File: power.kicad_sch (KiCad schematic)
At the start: 0 parts

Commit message: Setup charging
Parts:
- added BT1: Battery_Cell, Connector_JST:JST_PH_S2B-PH-K_1x02_P2.00mm_Horizontal, symbol Device:Battery_Cell
- added C7: C, symbol Device:C
- added C8, C9: 4.7u, symbol Device:C
- added D1: D, symbol Device:D
- added D2: LED, symbol Device:LED
- added F1: Fuse, symbol Device:Fuse
- added J2: USB_C_Receptacle, Connector_USB:USB_C_Receptacle_GCT_USB4105-xx-A_16P_TopMnt_Horizontal, symbol Connector:USB_C_Receptacle
- added Q1, Q2: Q_NMOS_GSD, Package_TO_SOT_SMD:TSOT-23, symbol Device:Q_NMOS_GSD
- added R1, R2: 5.1k, symbol Device:R
- added R3: 220, symbol Device:R
- added R4: 2k, symbol Device:R
- added R5: R, symbol Device:R
- added R6: 470, symbol Device:R
- added U2: ~, Package_TO_SOT_SMD:SOT-23-5, symbol generic:Battery_Management
- added U3: MCP73831-2-OT, Package_TO_SOT_SMD:SOT-23-5, symbol Battery_Management:MCP73831-2-OT
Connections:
- new net: D2.1 (K), R6.1
- new net: D2.2 (A), U3.1 (STAT)
- new net: Q2.1 (G), U2.4 (DO)
- new net: Q1.3 (D), Q2.3 (D)
- new net: R5.1, U3.5 (PROG)
- new net: J2.B5 (CC2), R2.1
- new net: R4.2, U2.1 (VM)
- new net: C7.1, R3.1, U2.2 (VDD)
- new net: BT1.2 (-), F1.2
- new net: J2.A5 (CC1), R1.1
- new net: Q1.1 (G), U2.5 (CO)
- new net +BATT: BT1.1 (+), C8.1, D1.1 (K), R3.2, U3.3 (V_{BAT})
- new net -BATT: C7.2, D1.2 (A), F1.1, Q2.2 (S), U2.3 (VSS)
- new net D+: J2.A6 (D+), J2.B6 (D+)
- new net D-: J2.A7 (D-), J2.B7 (D-)
- new net GND: C8.2, C9.2, J2.A1 (GND), J2.A12 (GND), J2.B1 (GND), J2.B12 (GND), Q1.2 (S), R1.2, R2.2, R4.1, R5.2, R6.2, U3.2 (V_{SS})
- new net VBUS: C9.1, J2.A4 (VBUS), J2.A9 (VBUS), J2.B4 (VBUS), J2.B9 (VBUS), U3.4 (V_{DD})

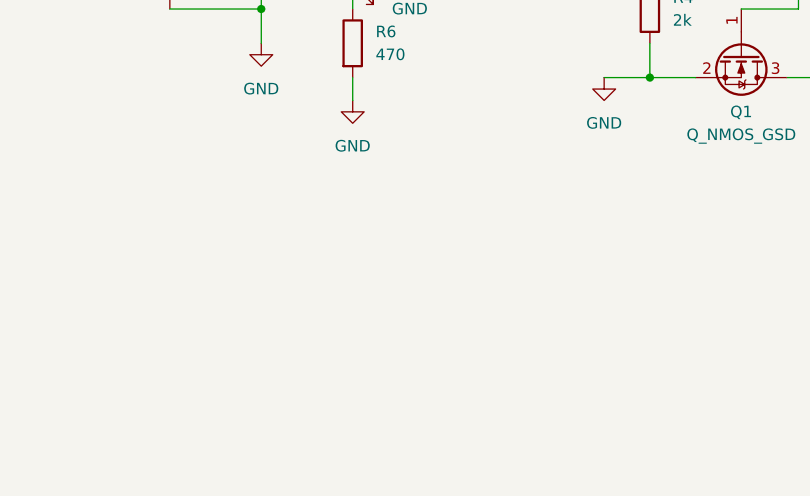
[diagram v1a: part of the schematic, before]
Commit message: Added outputs page
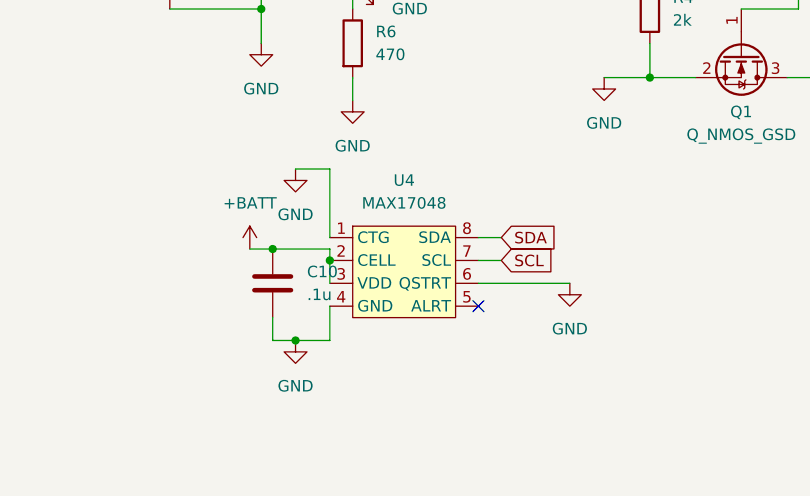
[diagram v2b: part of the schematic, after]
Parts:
- added C10: .1u, symbol Device:C
- added U4: MAX17048, Package_DFN_QFN:TDFN-8-1EP_2x2mm_P0.5mm_EP0.8x1.2mm, symbol generic:MAX17048
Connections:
- net +BATT: now also C10.1, U4.2 (CELL), U4.3 (VDD)
- net GND: now also C10.2, U4.1 (CTG), U4.4 (GND), U4.6 (QSTRT)
- new net SCL: U4.7 (SCL)
- new net SDA: U4.8 (SDA)
- no-connect marks 0 -> 1

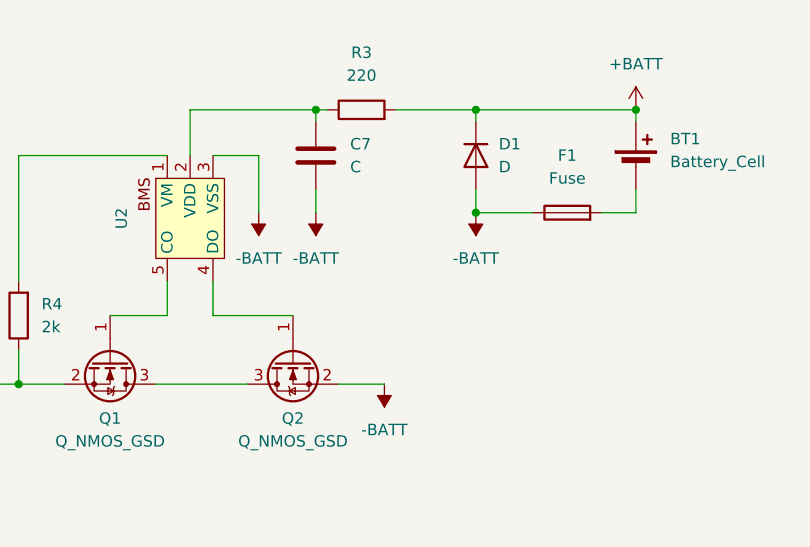
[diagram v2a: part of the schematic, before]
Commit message: Added output headers
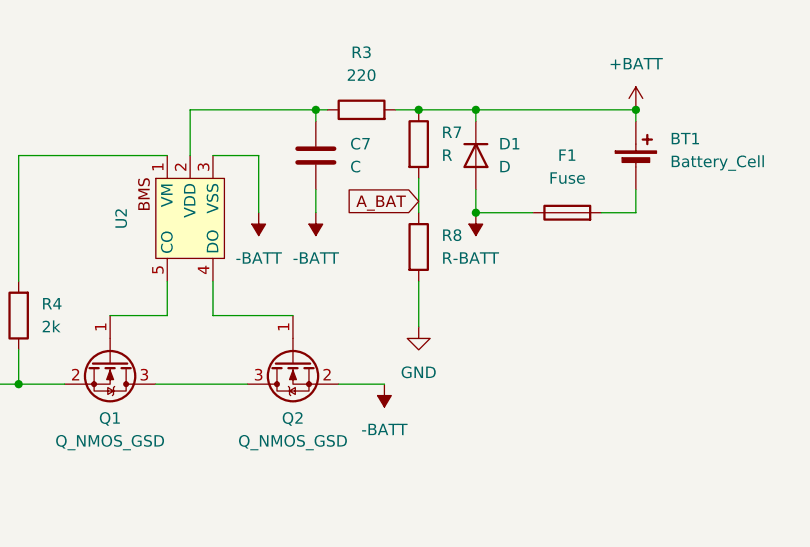
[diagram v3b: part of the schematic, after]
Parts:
- added R7, R8: R, symbol Device:R
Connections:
- net +BATT: now also R7.1
- net GND: now also R8.2
- new net A_BAT: R7.2, R8.1

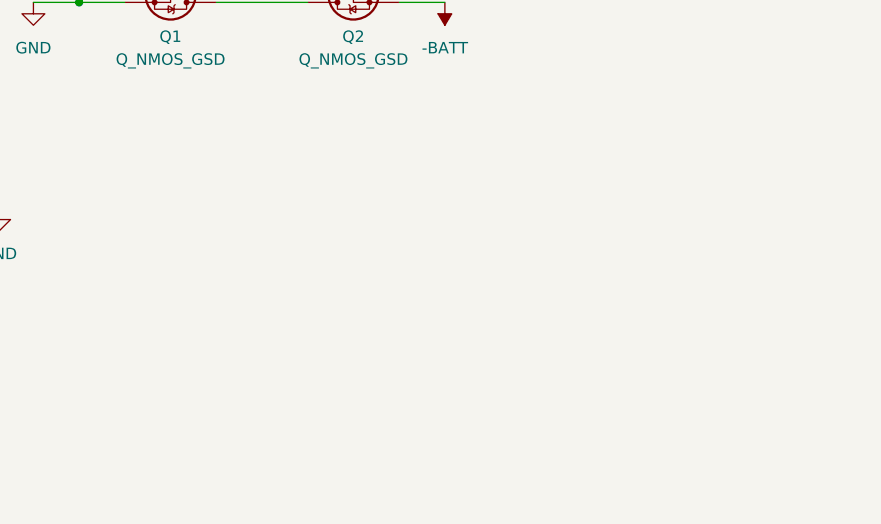
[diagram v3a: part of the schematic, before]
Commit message: Added pmos and regulator
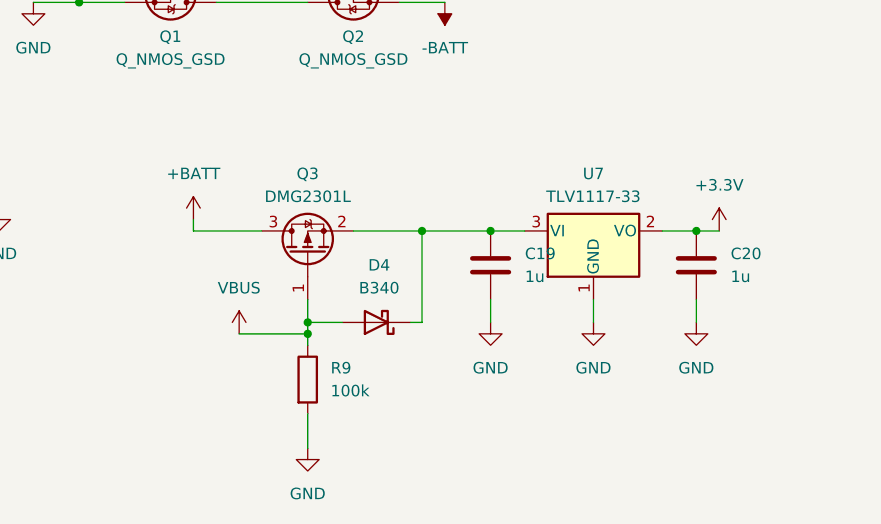
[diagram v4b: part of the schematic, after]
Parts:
- added C19, C20: 1u, symbol Device:C
- added D4: B340, Diode_SMD:D_SMC, symbol Diode:B340
- added Q3: DMG2301L, Package_TO_SOT_SMD:SOT-23, symbol Transistor_FET:DMG2301L
- added R9: 100k, symbol Device:R
- added U7: TLV1117-33, Package_TO_SOT_SMD:SOT-223-3_TabPin2, symbol Regulator_Linear:TLV1117-33
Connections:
- net +BATT: now also Q3.3 (D)
- net GND: now also C19.2, C20.2, R9.2, U7.1 (GND)
- net VBUS: now also D4.2 (A), Q3.1 (G), R9.1
- new net: C19.1, D4.1 (K), Q3.2 (S), U7.3 (VI)
- new net +3.3V: C20.1, U7.2 (VO)

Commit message: Switch regulator to 1.5A
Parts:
- removed U7: TLV1117-33, Package_TO_SOT_SMD:SOT-223-3_TabPin2, symbol Regulator_Linear:TLV1117-33
- added U8: LD39150DT33, Package_TO_SOT_SMD:TO-252-3_TabPin2, symbol Regulator_Linear:LD39150DT33
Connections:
- net +3.3V: now also U8.3 (VO)
- net GND: now also U8.2 (GND)
- net at C19.1, D4.1 (K), Q3.2 (S): now also U8.1 (VI)
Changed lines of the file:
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@@
-	)
-	(symbol
-		(lib_id "Regulator_Linear:TLV1117-33")
-		(at 226.06 87.63 0)
-		(unit 1)
-		(exclude_from_sim no)
-		(in_bom yes)
-		(on_board yes)
-		(dnp no)
-		(fields_autoplaced yes)
-		(property "Reference" "U7"
-			(at 226.06 81.28 0)
-			(effects
-				(font
-					(size 1.27 1.27)
-				)
-			)
-		)
-		(property "Value" "TLV1117-33"
-			(at 226.06 83.82 0)
-			(effects
-				(font
-					(size 1.27 1.27)
-				)
-			)
-		)
-		(property "Footprint" "Package_TO_SOT_SMD:SOT-223-3_TabPin2"
-			(at 226.06 87.63 0)
-			(effects
-				(font
-					(size 1.27 1.27)
-				)
-				(hide yes)
-			)
-		)
-		(property "Datasheet" "http://www.ti.com/lit/ds/symlink/tlv1117.pdf"
-			(at 226.06 87.63 0)
-			(effects
-				(font
-					(size 1.27 1.27)
-				)
-				(hide yes)
-			)
-		)
-		(property "Description" "800mA Low-Dropout Linear Regulator, 3.3V fixed output, TO-220/TO-252/TO-263/SOT-223"
-			(at 226.06 87.63 0)
-			(effects
-				(font
-					(size 1.27 1.27)
-				)
-				(hide yes)
-			)
-		)
-		(property "LCSC PN" "C15578"
-			(at 226.06 87.63 0)
-			(effects
-				(font
-					(size 1.27 1.27)
-				)
-				(hide yes)
-			)
-		)
-		(property "Part Number" "TLV1117LV33DCYR"
-			(at 226.06 87.63 0)
-			(effects
-				(font
-					(size 1.27 1.27)
-				)
-				(hide yes)
-			)
-		)
-		(pin "1"
-		)
-		(pin "3"
-		)
-		(pin "2"
-		)
-		(instances
-			(project ""
-				(path "/4b478080-1b18-4cae-a6eb-51454cf43595/0dd7376e-3e01-470b-b555-85887cf9232f"
-					(reference "U7")
-					(unit 1)
-				)
-			)
-		)
 	)
 	(symbol
@@
 					(unit 1)
 				)
+			)
+		)
+	)
+	(symbol
+		(lib_id "Regulator_Linear:LD39150DT33")
+		(at 226.06 87.63 0)
+		(unit 1)
+		(exclude_from_sim no)
+		(in_bom yes)
+		(on_board yes)
+		(dnp no)
+		(fields_autoplaced yes)
+		(property "Reference" "U8"
+			(at 226.06 81.28 0)
+			(effects
+				(font
+					(size 1.27 1.27)
+				)
+			)
+		)
+		(property "Value" "LD39150DT33"
+			(at 226.06 83.82 0)
+			(effects
+				(font
+					(size 1.27 1.27)
+				)
+			)
+		)
+		(property "Footprint" "Package_TO_SOT_SMD:TO-252-3_TabPin2"
+			(at 226.06 82.55 0)
+			(effects
+				(font
+					(size 1.27 1.27)
+				)
+				(hide yes)
+			)
+		)
+		(property "Datasheet" "https://www.st.com/resource/en/datasheet/ld39150.pdf"
+			(at 228.6 93.98 0)
+			(effects
+				(font
+					(size 1.27 1.27)
+				)
+				(hide yes)
+			)
+		)
+		(property "Description" "1.5A Ultra Low Dropout regulator, positive, 3.3V fixed output, TO-252"
+			(at 226.06 87.63 0)
+			(effects
+				(font
+					(size 1.27 1.27)
+				)
+				(hide yes)
+			)
+		)
+		(property "LCSC PN" "C155559"
+			(at 226.06 87.63 0)
+			(effects
+				(font
+					(size 1.27 1.27)
+				)
+				(hide yes)
+			)
+		)
+		(pin "2"
+		)
+		(pin "1"
+		)
+		(pin "3"
+		)
+		(instances
+			(project ""
+				(path "/4b478080-1b18-4cae-a6eb-51454cf43595/0dd7376e-3e01-470b-b555-85887cf9232f"
+					(reference "U8")
+					(unit 1)
+				)

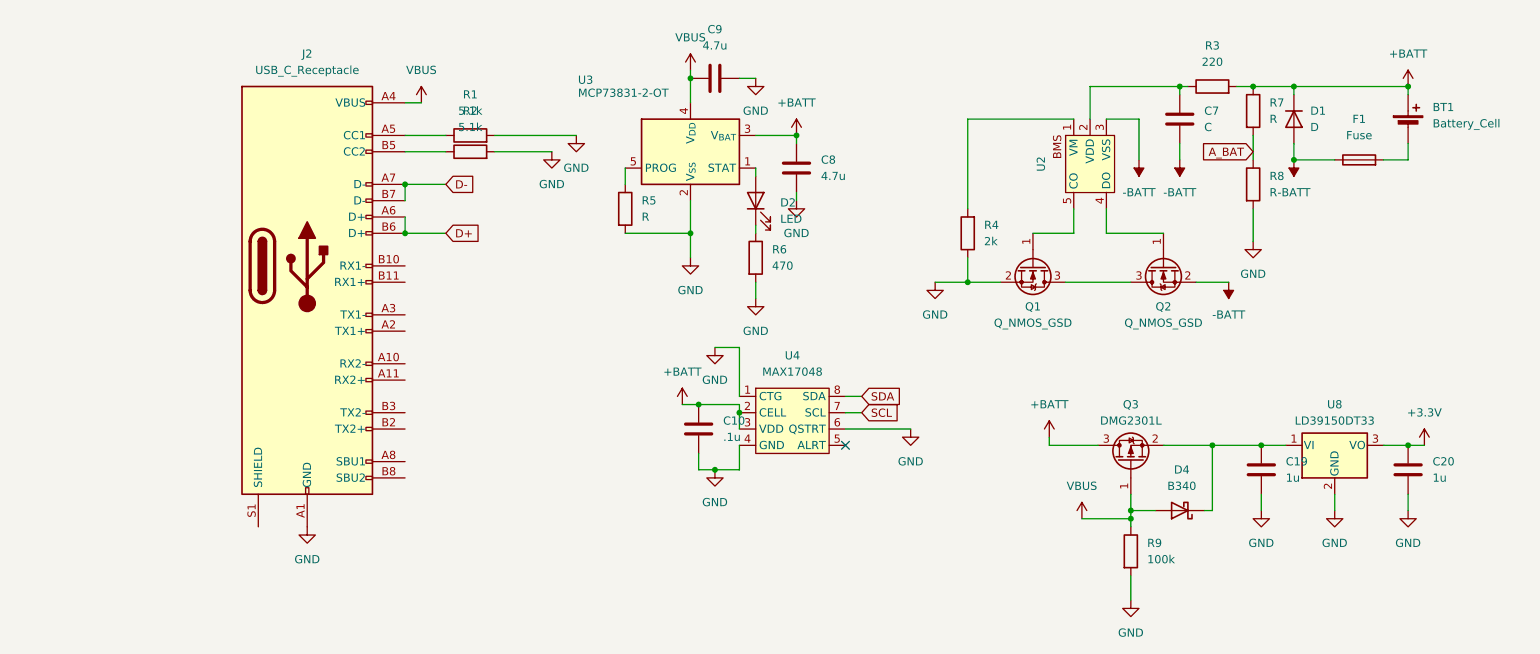
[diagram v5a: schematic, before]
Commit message: Added TVS diode
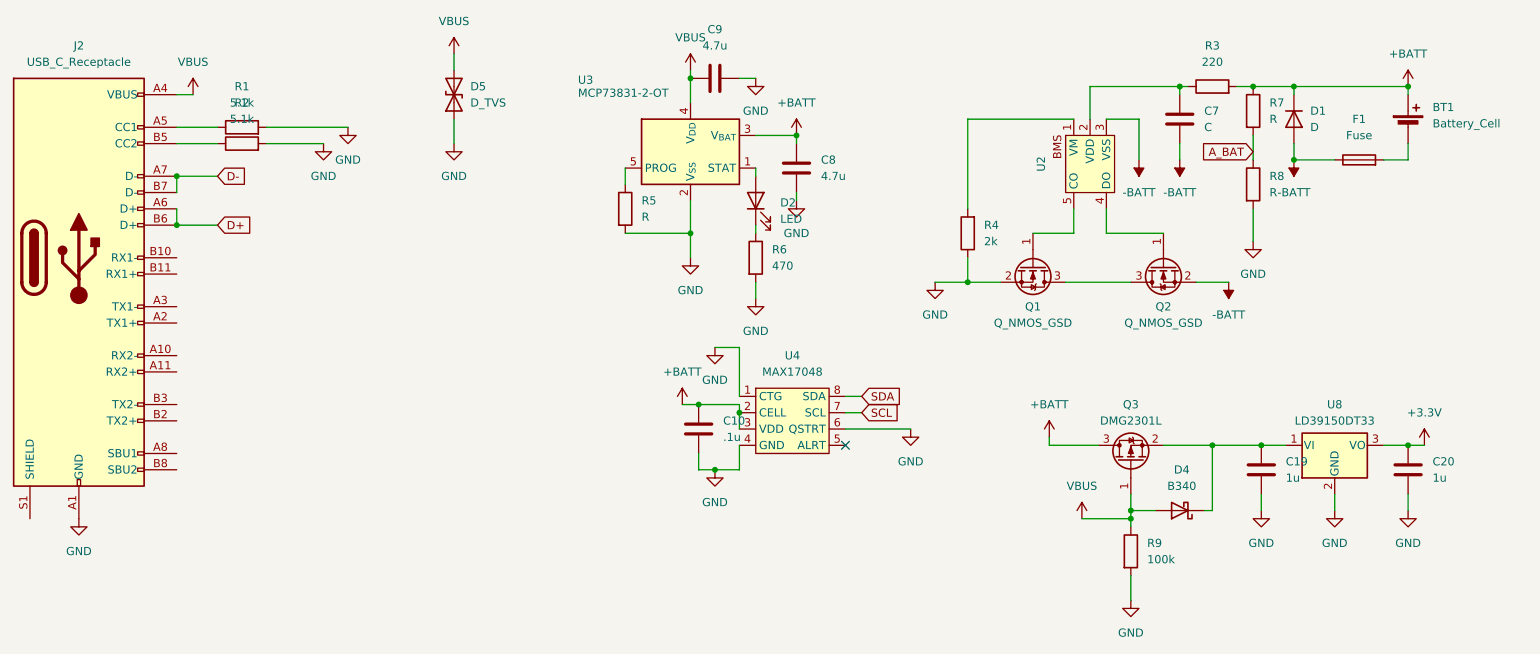
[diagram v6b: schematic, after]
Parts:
- added D5: D_TVS, Diode_SMD:D_0402_1005Metric, symbol Device:D_TVS
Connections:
- net GND: now also D5.1 (A1)
- net VBUS: now also D5.2 (A2)
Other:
- moved on the sheet: J2, R1, R2

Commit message: Added microphone, fuse
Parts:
- F1: footprint (none) -> Fuse:Fuse_1210_3225Metric; LCSC PN (none) -> C2982275; Part Number (none) -> Shenzhen JDT Fuse ASMD1210-150-16V
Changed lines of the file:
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@@
 		(on_board yes)
 		(dnp no)
-		(fields_autoplaced yes)
 		(property "Reference" "#PWR015"
 			(at 219.71 39.37 0)
@@
 			)
 		)
-		(property "Footprint" ""
+		(property "Footprint" "Fuse:Fuse_1210_3225Metric"
 			(at 229.87 44.958 90)
 			(effects
@@
 			(effects
 				(font
+					(size 1.27 1.27)
+				)
+				(hide yes)
+			)
+		)
+		(property "Part Number" "Shenzhen JDT Fuse ASMD1210-150-16V"
+			(at 229.87 43.18 90)
+			(effects
+				(font
+					(size 1.27 1.27)
+				)
+				(hide yes)
+			)
+		)
+		(property "LCSC PN" "C2982275"
+			(at 229.87 43.18 90)
+			(effects
+				(font

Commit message: finished schematic
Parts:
- removed D1: D, symbol Device:D
- added D1: B340, Diode_SMD:D_SMC, symbol Diode:B340
- C10: footprint (none) -> Capacitor_SMD:C_0603_1608Metric; LCSC PN (none) -> C14663
- C19, C20: footprint (none) -> Capacitor_SMD:C_0603_1608Metric; LCSC PN (none) -> C15849
- C7: value C -> .1u; footprint (none) -> Capacitor_SMD:C_0603_1608Metric; LCSC PN (none) -> C14663
- C8, C9: footprint (none) -> Capacitor_SMD:C_0603_1608Metric; LCSC PN (none) -> C19666
- D2: footprint (none) -> LED_SMD:LED_0805_2012Metric; LCSC PN (none) -> C965817
- F1: LCSC PN C2982275 -> C135349; Part Number Shenzhen JDT Fuse ASMD1210-150-16V -> Shenzhen JDT Fuse ASMD1210-075
- R1, R2: footprint (none) -> Resistor_SMD:R_0603_1608Metric; LCSC PN (none) -> C122969
- R3: footprint (none) -> Resistor_SMD:R_0603_1608Metric; LCSC PN (none) -> C107696
- R4: footprint (none) -> Resistor_SMD:R_0603_1608Metric; LCSC PN (none) -> C105576
- R5: value R -> 2k; footprint (none) -> Resistor_SMD:R_0603_1608Metric; LCSC PN (none) -> C105576
- R6: footprint (none) -> Resistor_SMD:R_0603_1608Metric; LCSC PN (none) -> C114669
- R7, R8: value R -> 100k; footprint (none) -> Resistor_SMD:R_0603_1608Metric; LCSC PN (none) -> C14675
- R9: footprint (none) -> Resistor_SMD:R_0603_1608Metric; LCSC PN (none) -> C14675
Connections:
- net +BATT: now also D1.1 (K)
- net -BATT: now also D1.2 (A)
